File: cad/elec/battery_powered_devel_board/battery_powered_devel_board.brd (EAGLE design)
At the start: 55 x 18 mm, 16 parts

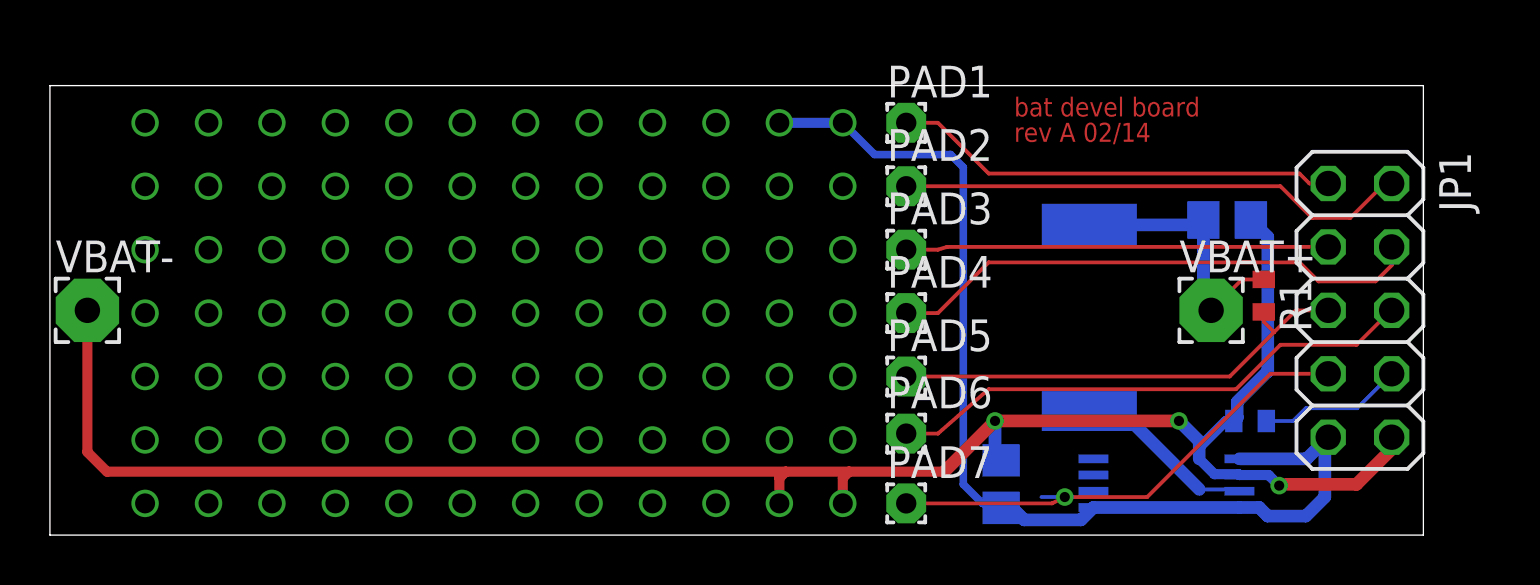
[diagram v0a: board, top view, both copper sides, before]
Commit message: changed battery sensing line on battery board to fit stm uc board
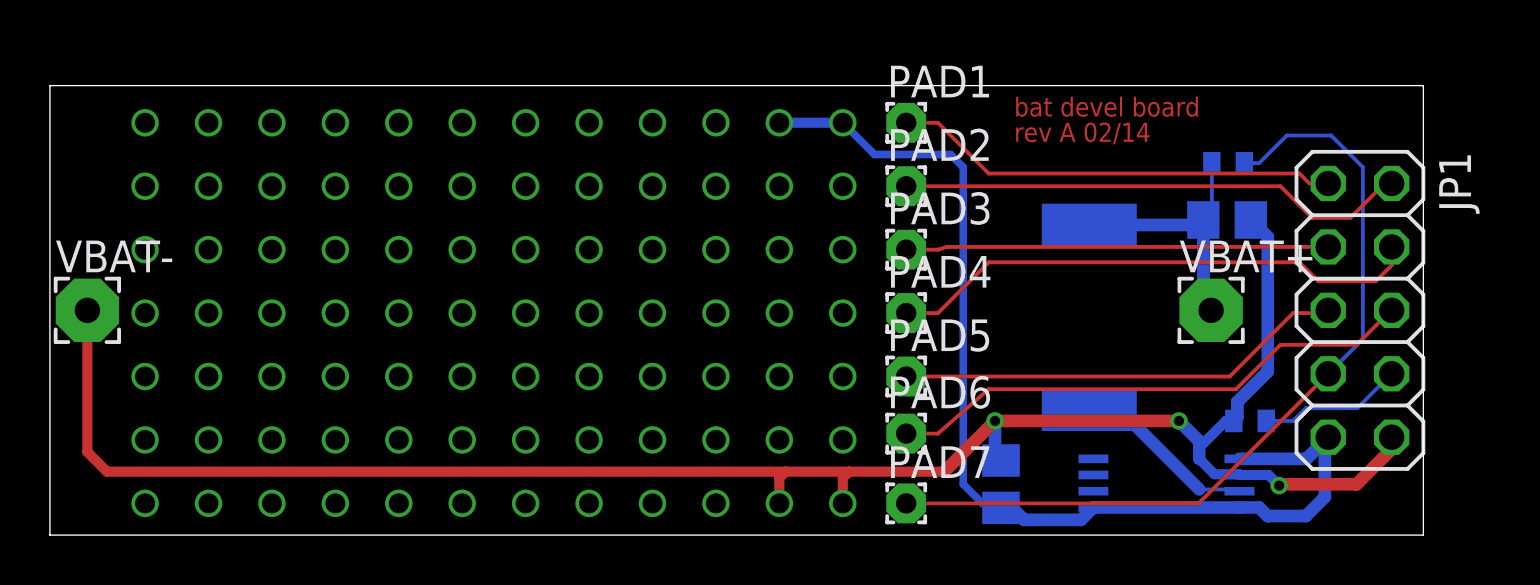
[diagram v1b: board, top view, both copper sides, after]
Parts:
- moved R1 5.49 mm to (47.2, 14.9), flipped to the bottom, turned to 180 degrees
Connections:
- net IO_4: no longer R1.2
- net IO_6: now also R1.2
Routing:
- net IO_6: track 19.9 -> 33.6 mm, vias 1 -> 0
- net IO_4: track 19.0 -> 18.0 mm
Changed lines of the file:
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@@
 <attribute name="DIGIKEY" value="1276-1100-1-ND" x="75.08" y="32.94" size="1.778" layer="28" rot="MR180" display="off"/>
 </element>
-<element name="R1" library="rcl" package="R0402" value="0" x="48.608" y="9.588" rot="R270">
-<attribute name="DIGIKEY" value="311-0.0JRCT-ND" x="21.938" y="-9.462" size="1.778" layer="27" rot="R270" display="off"/>
+<element name="R1" library="rcl" package="R0402" value="0" x="47.18" y="14.892" rot="MR180">
+<attribute name="DIGIKEY" value="311-0.0JRCT-ND" x="66.23" y="41.562" size="1.778" layer="28" rot="MR180" display="off"/>
 </element>
 <element name="R2" library="rcl" package="R0402" value="1M" x="48.06" y="4.57" rot="MR0">
@@
 <signal name="IO_4">
 <contactref element="JP1" pad="5"/>
-<wire x1="51.19" y1="9" x2="49.894" y2="9" width="0.1524" layer="1"/>
-<wire x1="49.894" y1="9" x2="49.022" y2="8.128" width="0.1524" layer="1"/>
-<wire x1="49.022" y1="8.128" x2="47.244" y2="6.35" width="0.1524" layer="1"/>
 <wire x1="47.244" y1="6.35" x2="34.29" y2="6.35" width="0.1524" layer="1"/>
 <contactref element="PAD5" pad="1"/>
-<contactref element="R1" pad="2"/>
-<wire x1="48.608" y1="8.938" x2="48.608" y2="8.542" width="0.1524" layer="1"/>
-<wire x1="48.608" y1="8.542" x2="49.022" y2="8.128" width="0.1524" layer="1"/>
+<wire x1="47.244" y1="6.35" x2="49.784" y2="8.89" width="0.1524" layer="1"/>
+<wire x1="49.784" y1="8.89" x2="51.08" y2="8.89" width="0.1524" layer="1"/>
+<wire x1="51.08" y1="8.89" x2="51.19" y2="9" width="0.1524" layer="1"/>
 </signal>
 <signal name="IO_6">
 <contactref element="JP1" pad="7"/>
-<wire x1="51.19" y1="6.46" x2="48.878" y2="6.46" width="0.1524" layer="1"/>
-<via x="40.64" y="1.524" extent="1-16" drill="0.4064"/>
-<wire x1="40.64" y1="1.524" x2="39.706" y2="1.524" width="0.1524" layer="16"/>
-<wire x1="34.29" y1="1.27" x2="40.132" y2="1.27" width="0.1524" layer="1"/>
-<wire x1="40.132" y1="1.27" x2="40.64" y2="1.524" width="0.1524" layer="1"/>
-<wire x1="48.878" y1="6.46" x2="43.942" y2="1.524" width="0.1524" layer="1"/>
-<wire x1="43.942" y1="1.524" x2="40.64" y2="1.524" width="0.1524" layer="1"/>
 <contactref element="PAD7" pad="1"/>
+<contactref element="R1" pad="2"/>
+<wire x1="34.29" y1="1.27" x2="46" y2="1.27" width="0.1524" layer="1"/>
+<wire x1="46" y1="1.27" x2="51.19" y2="6.46" width="0.1524" layer="1"/>
+<wire x1="47.83" y1="14.892" x2="48.42" y2="14.892" width="0.1524" layer="16"/>
+<wire x1="48.42" y1="14.892" x2="49.53" y2="16.002" width="0.1524" layer="16"/>
+<wire x1="49.53" y1="16.002" x2="51.308" y2="16.002" width="0.1524" layer="16"/>
+<wire x1="51.308" y1="16.002" x2="52.578" y2="14.732" width="0.1524" layer="16"/>
+<wire x1="52.578" y1="14.732" x2="52.578" y2="7.848" width="0.1524" layer="16"/>
+<wire x1="52.578" y1="7.848" x2="51.19" y2="6.46" width="0.1524" layer="16"/>
 </signal>
 <signal name="IO_1">
@@
 <wire x1="46.19" y1="9.31" x2="46.5" y2="9" width="0.508" layer="16"/>
 <contactref element="R1" pad="1"/>
-<wire x1="48.608" y1="10.238" x2="47.738" y2="10.238" width="0.1524" layer="1"/>
-<wire x1="47.738" y1="10.238" x2="46.5" y2="9" width="0.1524" layer="1"/>
+<wire x1="46.53" y1="14.892" x2="46.53" y2="12.96" width="0.1524" layer="16"/>
+<wire x1="46.53" y1="12.96" x2="46.19" y2="12.62" width="0.1524" layer="16"/>
 </signal>
 <signal name="N$5">
